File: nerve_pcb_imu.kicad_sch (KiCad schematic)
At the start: 13 parts, among them U4 BNO085, Y3 32k768

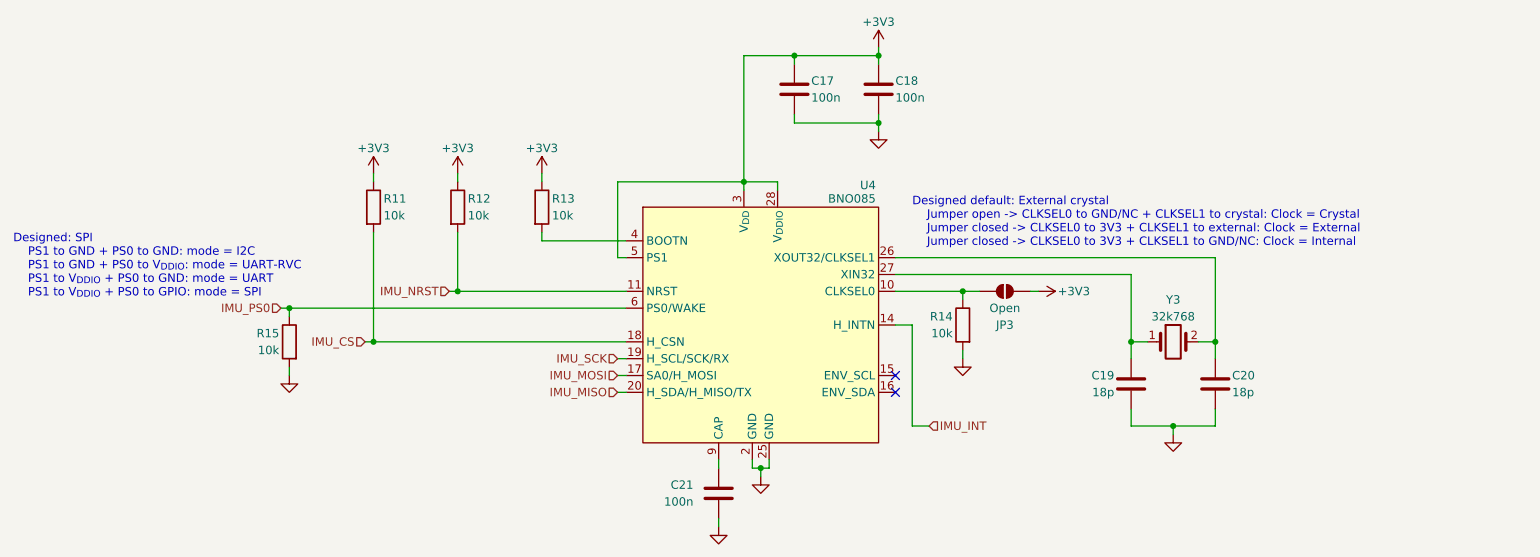
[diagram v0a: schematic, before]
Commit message: Fix BNO085 circuit and touchups
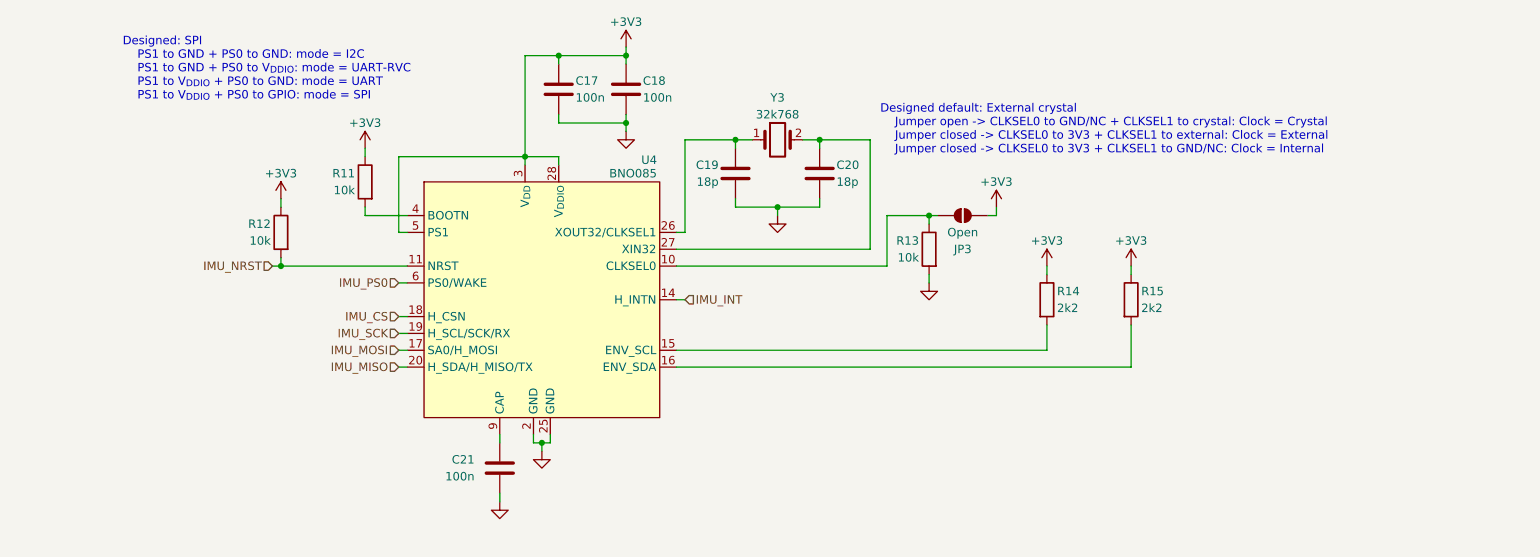
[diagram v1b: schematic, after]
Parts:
- removed R11: 10k, Resistor_SMD:R_0603_1608Metric, symbol Device:R
- added R14: 2k2, Resistor_SMD:R_0603_1608Metric, symbol Device:R
- R15: value 10k -> 2k2
- renumbered R13 to R11, R14 to R13
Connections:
- net +3V3: now also R15.1, R14.1
- net GND: no longer R15.2
- net IMU_PS0: no longer R15.1
- net at C20.1, Y3.2: now also U4.27 (XIN32); no longer U4.26 (XOUT32/CLKSEL1)
- net at U4.15 (ENV_SCL): now also R14.2
- net at U4.16 (ENV_SDA): now also R15.2
- net at C19.1, Y3.1: now also U4.26 (XOUT32/CLKSEL1); no longer U4.27 (XIN32)
- no-connect marks 2 -> 0
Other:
- moved on the sheet: C17, C18, C19, C20, C21, JP3, R11, R12, R13, U4, Y3

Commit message: Update for KiCad 9.0 and component library
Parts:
- U4: Distributor Link https://www.digikey.com/en/products/detail/ceva-technologie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 -> https://www.digikey.ca/en/products/detail/ceva-technologies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

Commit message: Add minor decoupling caps
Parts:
- renumbered C17 to C20, C18 to C21, C19 to C22, C20 to C23, C21 to C24
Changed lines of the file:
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@@
 		(on_board yes)
 		(dnp no)
-		(property "Reference" "C17"
+		(property "Reference" "C20"
 			(at 132.08 68.58 0)
 			(effects
@@
 			(project "nerve_pcb"
 				(path "/c0277862-b3f2-4e0e-986f-34702f0543f0/1178a2c5-f6af-4893-bc81-c8b9cb81f032"
-					(reference "C17")
+					(reference "C20")
 					(unit 1)
 				)
@@
 		(on_board yes)
 		(dnp no)
-		(property "Reference" "C20"
+		(property "Reference" "C23"
 			(at 171.45 81.28 0)
 			(effects
@@
 			(project "nerve_pcb"
 				(path "/c0277862-b3f2-4e0e-986f-34702f0543f0/1178a2c5-f6af-4893-bc81-c8b9cb81f032"
-					(reference "C20")
+					(reference "C23")
 					(unit 1)
 				)
@@
 		(dnp no)
 		(fields_autoplaced yes)
-		(property "Reference" "#PWR072"
+		(property "Reference" "#PWR075"
 			(at 120.65 138.43 0)
 			(effects
@@
 			(project "nerve_pcb"
 				(path "/c0277862-b3f2-4e0e-986f-34702f0543f0/1178a2c5-f6af-4893-bc81-c8b9cb81f032"
-					(reference "#PWR072")
+					(reference "#PWR075")
 					(unit 1)
 				)
@@
 		(on_board yes)
 		(dnp no)
-		(property "Reference" "C21"
+		(property "Reference" "C24"
 			(at 116.84 125.7299 0)
 			(effects
@@
 			(project ""
 				(path "/c0277862-b3f2-4e0e-986f-34702f0543f0/1178a2c5-f6af-4893-bc81-c8b9cb81f032"
-					(reference "C21")
+					(reference "C24")
 					(unit 1)
 				)
@@
 		(on_board yes)
 		(dnp no)
-		(property "Reference" "C18"
+		(property "Reference" "C21"
 			(at 142.24 68.58 0)
 			(effects
@@
 			(project "nerve_pcb"
 				(path "/c0277862-b3f2-4e0e-986f-34702f0543f0/1178a2c5-f6af-4893-bc81-c8b9cb81f032"
-					(reference "C18")
+					(reference "C21")
 					(unit 1)
 				)
@@
 		(on_board yes)
 		(dnp no)
-		(property "Reference" "#PWR066"
+		(property "Reference" "#PWR069"
 			(at 195.58 91.44 0)
 			(effects
@@
 			(project "nerve_pcb"
 				(path "/c0277862-b3f2-4e0e-986f-34702f0543f0/1178a2c5-f6af-4893-bc81-c8b9cb81f032"
-					(reference "#PWR066")
+					(reference "#PWR069")
 					(unit 1)
 				)
@@
 		(on_board yes)
 		(dnp no)
-		(property "Reference" "C19"
+		(property "Reference" "C22"
 			(at 153.67 81.28 0)
 			(effects
@@
 			(project "nerve_pcb"
 				(path "/c0277862-b3f2-4e0e-986f-34702f0543f0/1178a2c5-f6af-4893-bc81-c8b9cb81f032"
-					(reference "C19")
+					(reference "C22")
 					(unit 1)
 				)
@@
 		(on_board yes)
 		(dnp no)
-		(property "Reference" "#PWR065"
+		(property "Reference" "#PWR068"
 			(at 87.63 90.17 0)
 			(effects
@@
 			(project "nerve_pcb"
 				(path "/c0277862-b3f2-4e0e-986f-34702f0543f0/1178a2c5-f6af-4893-bc81-c8b9cb81f032"
-					(reference "#PWR065")
+					(reference "#PWR068")
 					(unit 1)
 				)
@@
 		(dnp no)
 		(fields_autoplaced yes)
-		(property "Reference" "#PWR071"
+		(property "Reference" "#PWR074"
 			(at 127 130.81 0)
 			(effects
@@
 			(project "nerve_pcb"
 				(path "/c0277862-b3f2-4e0e-986f-34702f0543f0/1178a2c5-f6af-4893-bc81-c8b9cb81f032"
-					(reference "#PWR071")
+					(reference "#PWR074")
 					(unit 1)
 				)
@@
 		(dnp no)
 		(fields_autoplaced yes)
-		(property "Reference" "#PWR070"
+		(property "Reference" "#PWR073"
 			(at 185.42 105.41 0)
 			(effects
@@
 			(project "nerve_pcb"
 				(path "/c0277862-b3f2-4e0e-986f-34702f0543f0/1178a2c5-f6af-4893-bc81-c8b9cb81f032"
-					(reference "#PWR070")
+					(reference "#PWR073")
 					(unit 1)
 				)
@@
 		(dnp no)
 		(fields_autoplaced yes)
-		(property "Reference" "#PWR063"
+		(property "Reference" "#PWR066"
 			(at 139.7 82.55 0)
 			(effects
@@
 			(project "nerve_pcb"
 				(path "/c0277862-b3f2-4e0e-986f-34702f0543f0/1178a2c5-f6af-4893-bc81-c8b9cb81f032"
-					(reference "#PWR063")
+					(reference "#PWR066")
 					(unit 1)
 				)
@@
 		(on_board yes)
 		(dnp no)
-		(property "Reference" "#PWR069"
+		(property "Reference" "#PWR072"
 			(at 215.9 100.33 0)
 			(effects
@@
 			(project "nerve_pcb"
 				(path "/c0277862-b3f2-4e0e-986f-34702f0543f0/1178a2c5-f6af-4893-bc81-c8b9cb81f032"
-					(reference "#PWR069")
+					(reference "#PWR072")
 					(unit 1)
 				)
@@
 		(on_board yes)
 		(dnp no)
-		(property "Reference" "#PWR068"
+		(property "Reference" "#PWR071"
 			(at 203.2 100.33 0)
 			(effects
@@
 			(project "nerve_pcb"
 				(path "/c0277862-b3f2-4e0e-986f-34702f0543f0/1178a2c5-f6af-4893-bc81-c8b9cb81f032"
-					(reference "#PWR068")
+					(reference "#PWR071")
 					(unit 1)
 				)
@@
 		(on_board yes)
 		(dnp no)
-		(property "Reference" "#PWR064"
+		(property "Reference" "#PWR067"
 			(at 100.33 82.55 0)
 			(effects
@@
 			(project "nerve_pcb"
 				(path "/c0277862-b3f2-4e0e-986f-34702f0543f0/1178a2c5-f6af-4893-bc81-c8b9cb81f032"
-					(reference "#PWR064")
+					(reference "#PWR067")
 					(unit 1)
 				)
@@
 		(dnp no)
 		(fields_autoplaced yes)
-		(property "Reference" "#PWR067"
+		(property "Reference" "#PWR070"
 			(at 162.56 95.25 0)
 			(effects
@@
 			(project "nerve_pcb"
 				(path "/c0277862-b3f2-4e0e-986f-34702f0543f0/1178a2c5-f6af-4893-bc81-c8b9cb81f032"
-					(reference "#PWR067")
+					(reference "#PWR070")
 					(unit 1)
 				)
@@
 		(on_board yes)
 		(dnp no)
-		(property "Reference" "#PWR062"
+		(property "Reference" "#PWR065"
 			(at 139.7 67.31 0)
 			(effects
@@
 			(project "nerve_pcb"
 				(path "/c0277862-b3f2-4e0e-986f-34702f0543f0/1178a2c5-f6af-4893-bc81-c8b9cb81f032"
-					(reference "#PWR062")
-					(unit 1)
-				)
+					(reference "#PWR065")
+					(unit 1)
+				)

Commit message: Add WS2812B decoupling caps and PCB cleanup
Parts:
- renumbered C20 to C22, C21 to C23, C22 to C24, C23 to C25, C24 to C26
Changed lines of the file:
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@@
 		(on_board yes)
 		(dnp no)
-		(property "Reference" "C20"
+		(property "Reference" "C22"
 			(at 132.08 68.58 0)
 			(effects
@@
 			(project "nerve_pcb"
 				(path "/c0277862-b3f2-4e0e-986f-34702f0543f0/1178a2c5-f6af-4893-bc81-c8b9cb81f032"
-					(reference "C20")
+					(reference "C22")
 					(unit 1)
 				)
@@
 		(on_board yes)
 		(dnp no)
-		(property "Reference" "C23"
+		(property "Reference" "C25"
 			(at 171.45 81.28 0)
 			(effects
@@
 			(project "nerve_pcb"
 				(path "/c0277862-b3f2-4e0e-986f-34702f0543f0/1178a2c5-f6af-4893-bc81-c8b9cb81f032"
-					(reference "C23")
+					(reference "C25")
 					(unit 1)
 				)
@@
 		(dnp no)
 		(fields_autoplaced yes)
-		(property "Reference" "#PWR075"
+		(property "Reference" "#PWR077"
 			(at 120.65 138.43 0)
 			(effects
@@
 			(project "nerve_pcb"
 				(path "/c0277862-b3f2-4e0e-986f-34702f0543f0/1178a2c5-f6af-4893-bc81-c8b9cb81f032"
-					(reference "#PWR075")
+					(reference "#PWR077")
 					(unit 1)
 				)
@@
 		(on_board yes)
 		(dnp no)
-		(property "Reference" "C24"
+		(property "Reference" "C26"
 			(at 116.84 125.7299 0)
 			(effects
@@
 			(project ""
 				(path "/c0277862-b3f2-4e0e-986f-34702f0543f0/1178a2c5-f6af-4893-bc81-c8b9cb81f032"
-					(reference "C24")
+					(reference "C26")
 					(unit 1)
 				)
@@
 		(on_board yes)
 		(dnp no)
-		(property "Reference" "C21"
+		(property "Reference" "C23"
 			(at 142.24 68.58 0)
 			(effects
@@
 			(project "nerve_pcb"
 				(path "/c0277862-b3f2-4e0e-986f-34702f0543f0/1178a2c5-f6af-4893-bc81-c8b9cb81f032"
-					(reference "C21")
+					(reference "C23")
 					(unit 1)
 				)
@@
 		(on_board yes)
 		(dnp no)
-		(property "Reference" "#PWR069"
+		(property "Reference" "#PWR071"
 			(at 195.58 91.44 0)
 			(effects
@@
 			(project "nerve_pcb"
 				(path "/c0277862-b3f2-4e0e-986f-34702f0543f0/1178a2c5-f6af-4893-bc81-c8b9cb81f032"
-					(reference "#PWR069")
+					(reference "#PWR071")
 					(unit 1)
 				)
@@
 		(on_board yes)
 		(dnp no)
-		(property "Reference" "C22"
+		(property "Reference" "C24"
 			(at 153.67 81.28 0)
 			(effects
@@
 			(project "nerve_pcb"
 				(path "/c0277862-b3f2-4e0e-986f-34702f0543f0/1178a2c5-f6af-4893-bc81-c8b9cb81f032"
-					(reference "C22")
+					(reference "C24")
 					(unit 1)
 				)
@@
 		(on_board yes)
 		(dnp no)
-		(property "Reference" "#PWR068"
+		(property "Reference" "#PWR070"
 			(at 87.63 90.17 0)
 			(effects
@@
 			(project "nerve_pcb"
 				(path "/c0277862-b3f2-4e0e-986f-34702f0543f0/1178a2c5-f6af-4893-bc81-c8b9cb81f032"
-					(reference "#PWR068")
+					(reference "#PWR070")
 					(unit 1)
 				)
@@
 		(dnp no)
 		(fields_autoplaced yes)
-		(property "Reference" "#PWR074"
+		(property "Reference" "#PWR076"
 			(at 127 130.81 0)
 			(effects
@@
 			(project "nerve_pcb"
 				(path "/c0277862-b3f2-4e0e-986f-34702f0543f0/1178a2c5-f6af-4893-bc81-c8b9cb81f032"
-					(reference "#PWR074")
+					(reference "#PWR076")
 					(unit 1)
 				)
@@
 		(dnp no)
 		(fields_autoplaced yes)
-		(property "Reference" "#PWR073"
+		(property "Reference" "#PWR075"
 			(at 185.42 105.41 0)
 			(effects
@@
 			(project "nerve_pcb"
 				(path "/c0277862-b3f2-4e0e-986f-34702f0543f0/1178a2c5-f6af-4893-bc81-c8b9cb81f032"
-					(reference "#PWR073")
+					(reference "#PWR075")
 					(unit 1)
 				)
@@
 		(dnp no)
 		(fields_autoplaced yes)
-		(property "Reference" "#PWR066"
+		(property "Reference" "#PWR068"
 			(at 139.7 82.55 0)
 			(effects
@@
 			(project "nerve_pcb"
 				(path "/c0277862-b3f2-4e0e-986f-34702f0543f0/1178a2c5-f6af-4893-bc81-c8b9cb81f032"
-					(reference "#PWR066")
+					(reference "#PWR068")
 					(unit 1)
 				)
@@
 		(on_board yes)
 		(dnp no)
-		(property "Reference" "#PWR072"
+		(property "Reference" "#PWR074"
 			(at 215.9 100.33 0)
 			(effects
@@
 			(project "nerve_pcb"
 				(path "/c0277862-b3f2-4e0e-986f-34702f0543f0/1178a2c5-f6af-4893-bc81-c8b9cb81f032"
-					(reference "#PWR072")
+					(reference "#PWR074")
 					(unit 1)
 				)
@@
 		(on_board yes)
 		(dnp no)
-		(property "Reference" "#PWR071"
+		(property "Reference" "#PWR073"
 			(at 203.2 100.33 0)
 			(effects
@@
 			(project "nerve_pcb"
 				(path "/c0277862-b3f2-4e0e-986f-34702f0543f0/1178a2c5-f6af-4893-bc81-c8b9cb81f032"
-					(reference "#PWR071")
+					(reference "#PWR073")
 					(unit 1)
 				)
@@
 		(on_board yes)
 		(dnp no)
-		(property "Reference" "#PWR067"
+		(property "Reference" "#PWR069"
 			(at 100.33 82.55 0)
 			(effects
@@
 			(project "nerve_pcb"
 				(path "/c0277862-b3f2-4e0e-986f-34702f0543f0/1178a2c5-f6af-4893-bc81-c8b9cb81f032"
-					(reference "#PWR067")
+					(reference "#PWR069")
 					(unit 1)
 				)
@@
 		(dnp no)
 		(fields_autoplaced yes)
-		(property "Reference" "#PWR070"
+		(property "Reference" "#PWR072"
 			(at 162.56 95.25 0)
 			(effects
@@
 			(project "nerve_pcb"
 				(path "/c0277862-b3f2-4e0e-986f-34702f0543f0/1178a2c5-f6af-4893-bc81-c8b9cb81f032"
-					(reference "#PWR070")
+					(reference "#PWR072")
 					(unit 1)
 				)
@@
 		(on_board yes)
 		(dnp no)
-		(property "Reference" "#PWR065"
+		(property "Reference" "#PWR067"
 			(at 139.7 67.31 0)
 			(effects
@@
 			(project "nerve_pcb"
 				(path "/c0277862-b3f2-4e0e-986f-34702f0543f0/1178a2c5-f6af-4893-bc81-c8b9cb81f032"
-					(reference "#PWR065")
-					(unit 1)
-				)
+					(reference "#PWR067")
+					(unit 1)
+				)
